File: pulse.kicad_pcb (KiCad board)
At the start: 2 copper layers, 93.7 x 37.9 mm, 87 parts, among them J1 D-, J10 OUT_12V, J11 OUT_24V, J12 OUT_5V, J13 USB4085-GF-A_REVA, J2 D+, J3 OUT_VUSB, J4 Conn_01x05_Male, J5 EN_3v3, J6 EN_5V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

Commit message: Change PCB version Number
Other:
- board text added: "V0.1.0 Pre"
- board text removed: "V0.0.1 Pre"
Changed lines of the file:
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@@
-(kicad_pcb (version 20171130) (host pcbnew "(5.1.5-0-10_14)")
+(kicad_pcb (version 20171130) (host pcbnew 5.1.5-52549c5~84~ubuntu19.10.1)
   (general
     (thickness 1.6)
@@
   )
   (setup
-    (last_trace_width 1.5)
+    (last_trace_width 0.25)
     (user_trace_width 0.5)
     (user_trace_width 0.75)
@@
     (add_net "Net-(F1-Pad2)")
     (add_net "Net-(J13-PadA5)")
-    (add_net "Net-(J13-PadA8)")
     (add_net "Net-(J13-PadB5)")
-    (add_net "Net-(J13-PadB8)")
     (add_net "Net-(J5-Pad1)")
     (add_net "Net-(J6-Pad1)")
@@
     (add_net "Net-(R4-Pad1)")
     (add_net "Net-(R5-Pad2)")
-    (add_net "Net-(SW1-Pad3)")
-    (add_net "Net-(U1-Pad6)")
     (add_net VDC)
     (add_net VFB_3v3)
@@
     (effects (font (size 1 1) (thickness 0.15)) (justify mirror))
   )
-  (gr_text "V0.0.1 Pre" (at 185.2676 76.1492) (layer F.SilkS)
+  (gr_text "V0.1.0 Pre" (at 185.2676 76.1492) (layer F.SilkS)
     (effects (font (size 0.6 0.6) (thickness 0.15) italic))
   )

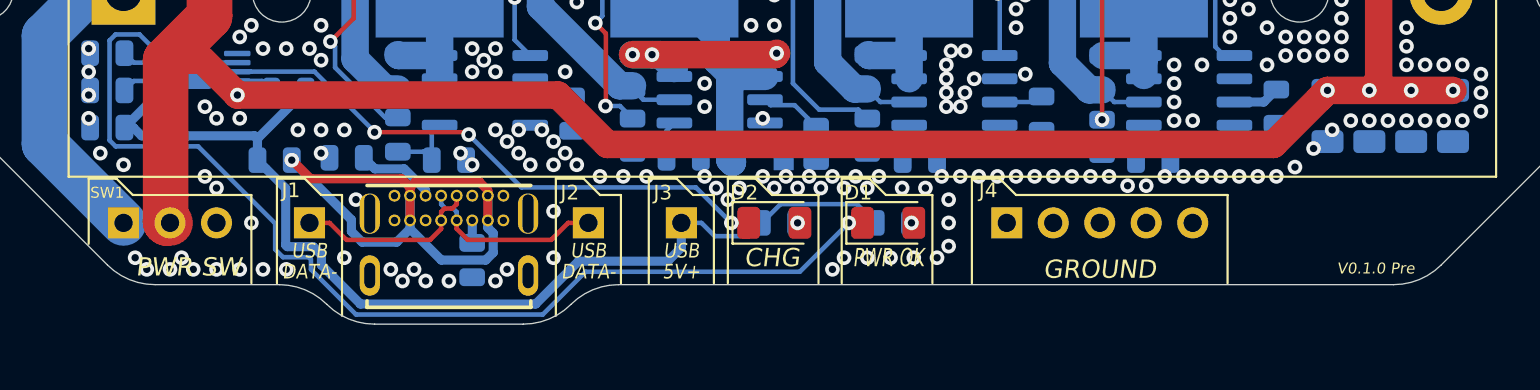
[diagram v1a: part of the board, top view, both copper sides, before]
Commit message: Add batteryless operation jumper pads
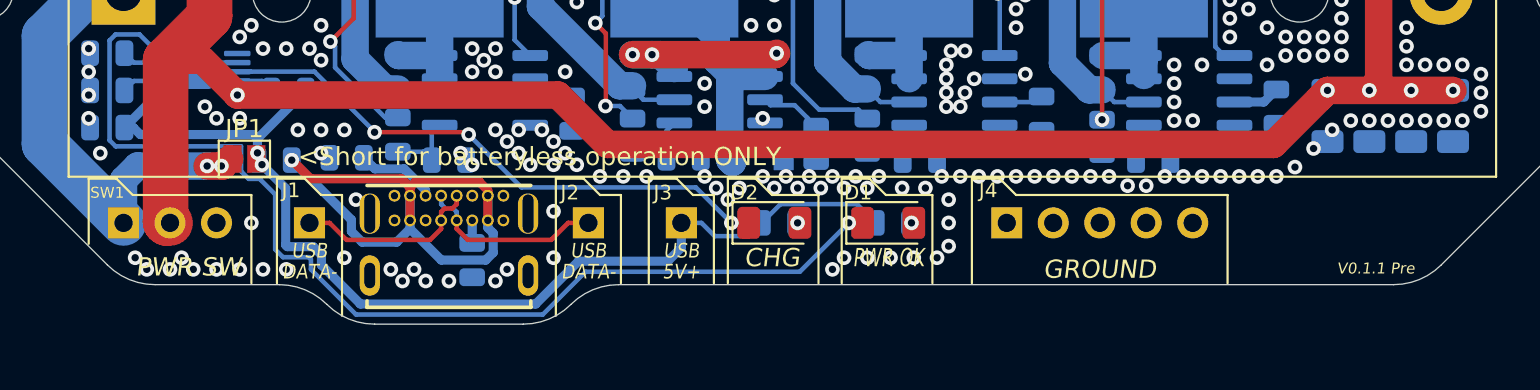
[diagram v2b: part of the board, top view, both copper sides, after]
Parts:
- added JP1: NoBattery, Jumper:SolderJumper-2_P1.3mm_Open_Pad1.0x1.5mm, F.Cu at (123.4, 70.2)
- C6: value 1500pF -> 470pF
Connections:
- J13 pad A8: (no net) -> Net-(J13-PadA8)
- J13 pad B8: (no net) -> Net-(J13-PadB8)
- SW1 pad 3: (no net) -> Net-(SW1-Pad3)
- U1 pad 6: (no net) -> Net-(U1-Pad6)
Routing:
- net Net-(BT1-Pad1): track 17.4 -> 26.8 mm, vias 0 -> 2
- net Net-(D1-Pad1): track 57.0 -> 58.8 mm
- net +5V: vias 0 -> 2
- net GND: vias 398 -> 395
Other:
- board text added: "<Short for batteryless operation ONLY"
- board text added: "V0.1.1 Pre"
- board text removed: "V0.1.0 Pre"

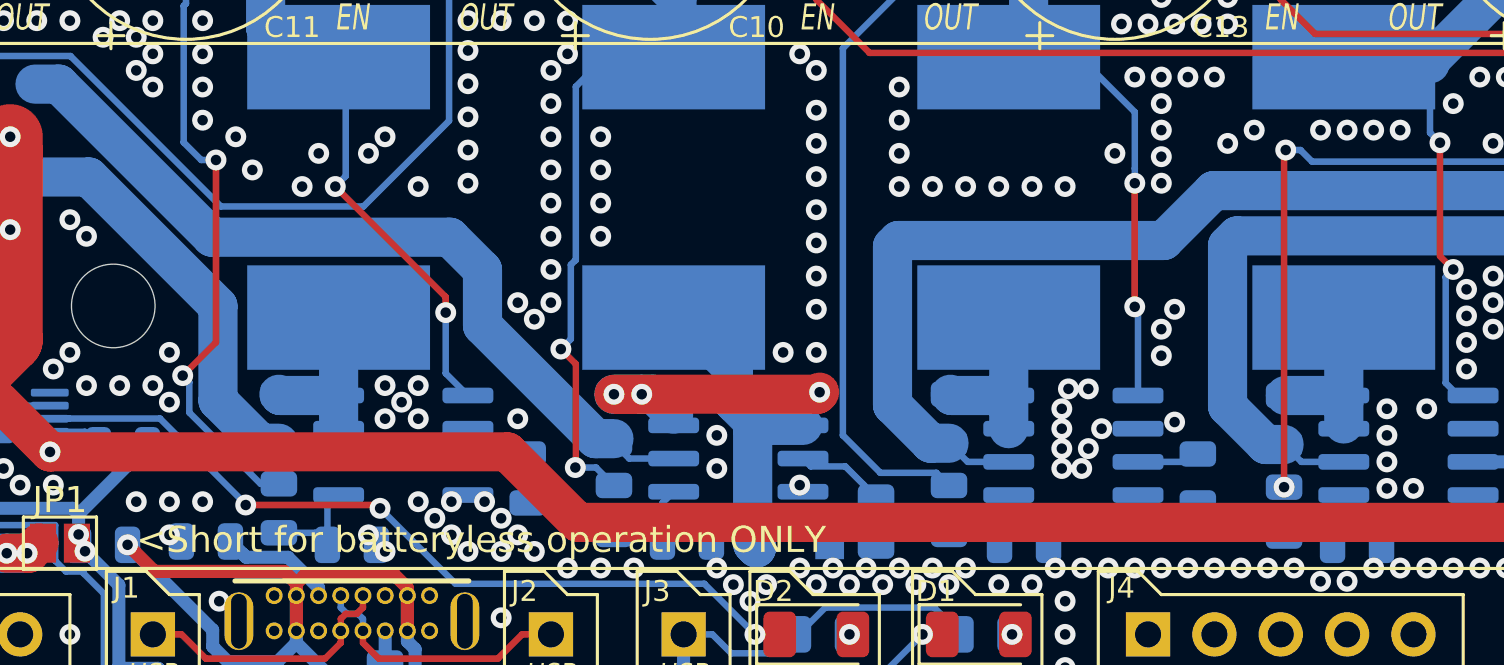
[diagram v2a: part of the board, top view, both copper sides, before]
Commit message: Change 0.22R shunt resistors to 1206
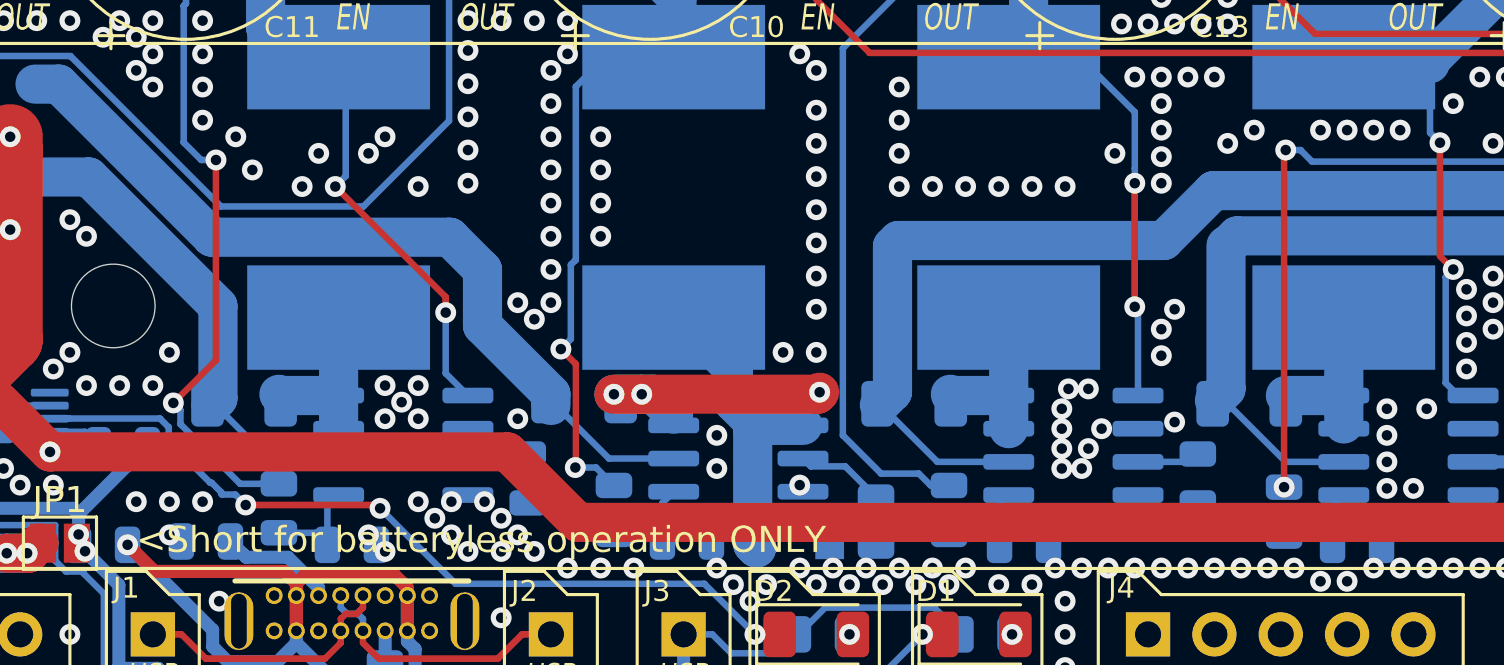
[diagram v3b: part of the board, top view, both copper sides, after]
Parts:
- R16, R17, R18, R19: footprint Resistor_SMD:R_0805_2012Metric -> Resistor_SMD:R_1206_3216Metric
- moved R18 1.47 mm to (169.0, 64.8), turned to 0 degrees
- moved R17 1.45 mm to (130.5, 64.8), turned to 0 degrees
- moved R19 1.45 mm to (156.1, 64.8), turned to 0 degrees
- moved R16 1.34 mm to (143.5, 64.7), turned to 0 degrees
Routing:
- net Net-(C11-Pad1): track 37.1 -> 38.6 mm
- net Net-(Q4-Pad2): track 42.3 -> 43.1 mm
- net Net-(Q2-Pad2): track 18.3 -> 18.9 mm
- net Net-(Q3-Pad2): track 28.0 -> 28.5 mm
- net GND: vias 395 -> 394
